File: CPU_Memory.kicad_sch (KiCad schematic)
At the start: 1 part

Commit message: Added LGA1151 socket bracket holes
stolen from another lga1151 footprint that has wrong pin numbers....
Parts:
- JCPU1: footprint A-my-stuff:LGA-1151_L47.1-W42.5-P0.91_PE115127-4041-01H -> A-my-stuff:LGA1151_TE-2287402-1
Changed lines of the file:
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@@
 			)
 		)
-		(property "Footprint" "A-my-stuff:LGA-1151_L47.1-W42.5-P0.91_PE115127-4041-01H"
+		(property "Footprint" "A-my-stuff:LGA1151_TE-2287402-1"
 			(at 107.95 246.38 0)
 			(effects
@@
 			)
 		)
-		(property "Footprint" "A-my-stuff:LGA-1151_L47.1-W42.5-P0.91_PE115127-4041-01H"
+		(property "Footprint" "A-my-stuff:LGA1151_TE-2287402-1"
 			(at 273.05 246.38 0)
 			(effects

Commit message: Added CPU CFG resistors
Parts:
- JCPU1: footprint A-my-stuff:LGA1151_TE-2287402-1 -> A-my-stuff:LGA-1151_L47.1-W42.5-P0.91_PE115127-4041-01H
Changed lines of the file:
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@@
 			)
 		)
-		(property "Footprint" "A-my-stuff:LGA1151_TE-2287402-1"
+		(property "Footprint" "A-my-stuff:LGA-1151_L47.1-W42.5-P0.91_PE115127-4041-01H"
 			(at 107.95 246.38 0)
 			(effects
@@
 			)
 		)
-		(property "Footprint" "A-my-stuff:LGA1151_TE-2287402-1"
+		(property "Footprint" "A-my-stuff:LGA-1151_L47.1-W42.5-P0.91_PE115127-4041-01H"
 			(at 273.05 246.38 0)
 			(effects

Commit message: stroopwafel.exe
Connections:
- net DDR4_CH1_A0: now also JCPU1.AW15 (DDR0_MA_0); no longer JCPU1.AL19 (DDR1_MA_0)
- net DDR4_CH1_A1: now also JCPU1.AU18 (DDR0_MA_1); no longer JCPU1.AL22 (DDR1_MA_1)
- net DDR4_CH1_A10: now also JCPU1.AY14 (DDR0_MA_10); no longer JCPU1.AP18 (DDR1_MA_10)
- net DDR4_CH1_A11: now also JCPU1.AU22 (DDR0_MA_11); no longer JCPU1.AU27 (DDR1_MA_11)
- net DDR4_CH1_A12: now also JCPU1.AV22 (DDR0_MA_12); no longer JCPU1.AV27 (DDR1_MA_12)
- net DDR4_CH1_A13: now also JCPU1.AV12 (DDR0_MA_13); no longer JCPU1.AR15 (DDR1_MA_13)
- net DDR4_CH1_A14_WE#: now also JCPU1.AV14 (DDR0_MA_14); no longer JCPU1.AL17 (DDR1_MA_14)
- net DDR4_CH1_A15_CAS#: now also JCPU1.AY11 (DDR0_MA_15); no longer JCPU1.AP16 (DDR1_MA_15)
- net DDR4_CH1_A16_RAS#: now also JCPU1.AW13 (DDR0_MA_16); no longer JCPU1.AN18 (DDR1_MA_16)
- net DDR4_CH1_A2: now also JCPU1.AU17 (DDR0_MA_2); no longer JCPU1.AM22 (DDR1_MA_2)
- net DDR4_CH1_A3: now also JCPU1.AV19 (DDR0_MA_3); no longer JCPU1.AM23 (DDR1_MA_3)
- net DDR4_CH1_A4: now also JCPU1.AT19 (DDR0_MA_4); no longer JCPU1.AP23 (DDR1_MA_4)
- net DDR4_CH1_A5: now also JCPU1.AU20 (DDR0_MA_5); no longer JCPU1.AL23 (DDR1_MA_5)
- net DDR4_CH1_A6: now also JCPU1.AV20 (DDR0_MA_6); no longer JCPU1.AW26 (DDR1_MA_6)
- net DDR4_CH1_A7: now also JCPU1.AU21 (DDR0_MA_7); no longer JCPU1.AY26 (DDR1_MA_7)
- net DDR4_CH1_A8: now also JCPU1.AT20 (DDR0_MA_8); no longer JCPU1.AU26 (DDR1_MA_8)
- net DDR4_CH1_A9: now also JCPU1.AT22 (DDR0_MA_9); no longer JCPU1.AW27 (DDR1_MA_9)
- net DDR4_CH1_ACT#: now also JCPU1.AU24 (DDR0_ACT#); no longer JCPU1.AU28 (DDR1_ACT#)
- net DDR4_CH1_Alert#: now also JCPU1.AT23 (DDR0_ALERT#); no longer JCPU1.AY25 (DDR1_ALERT#)
- net DDR4_CH1_BA0: now also JCPU1.AY13 (DDR0_BA_0); no longer JCPU1.AL18 (DDR1_BA_0)
- net DDR4_CH1_BA1: now also JCPU1.AV15 (DDR0_BA_1); no longer JCPU1.AM18 (DDR1_BA_1)
- net DDR4_CH1_BG0: now also JCPU1.AW23 (DDR0_BG_0); no longer JCPU1.AW28 (DDR1_BG_0)
- net DDR4_CH1_BG1: now also JCPU1.AV23 (DDR0_BG_1); no longer JCPU1.AY28 (DDR1_BG_1)
- net DDR4_CH1_CKE0: now also JCPU1.AY24 (DDR0_CKE_0); no longer JCPU1.AY29 (DDR1_CKE_0)
- net DDR4_CH1_CKE1: now also JCPU1.AW24 (DDR0_CKE_1); no longer JCPU1.AV29 (DDR1_CKE_1)
- net DDR4_CH1_CLK0+: now also JCPU1.AW18 (DDR0_CKP_0); no longer JCPU1.AM20 (DDR1_CKP_0)
- net DDR4_CH1_CLK0-: now also JCPU1.AV18 (DDR0_CKN_0); no longer JCPU1.AM21 (DDR1_CKN_0)
- net DDR4_CH1_CLK1+: now also JCPU1.AW17 (DDR0_CKP_1); no longer JCPU1.AP22 (DDR1_CKP_1)
- net DDR4_CH1_CLK1-: now also JCPU1.AY17 (DDR0_CKN_1); no longer JCPU1.AP21 (DDR1_CKN_1)
- net DDR4_CH1_CS0#: now also JCPU1.AW12 (DDR0_CS#_0); no longer JCPU1.AP17 (DDR1_CS#_0)
- net DDR4_CH1_CS1#: now also JCPU1.AU11 (DDR0_CS#_1); no longer JCPU1.AN15 (DDR1_CS#_1)
- net DDR4_CH1_DQ0: now also JCPU1.AE38 (DDR0_DQ_0/DDR0_DQ_0); no longer JCPU1.AD34 (DDR1_DQ_0/DDR0_DQ_16)
- net DDR4_CH1_DQ1: now also JCPU1.AE37 (DDR0_DQ_1/DDR0_DQ_1); no longer JCPU1.AD35 (DDR1_DQ_1/DDR0_DQ_17)
- net DDR4_CH1_DQ10: now also JCPU1.AL38 (DDR0_DQ_10/DDR0_DQ_10); no longer JCPU1.AK32 (DDR1_DQ_10/DDR0_DQ_26)
- net DDR4_CH1_DQ11: now also JCPU1.AL37 (DDR0_DQ_11/DDR0_DQ_11); no longer JCPU1.AL32 (DDR1_DQ_11/DDR0_DQ_27)
- net DDR4_CH1_DQ12: now also JCPU1.AJ40 (DDR0_DQ_12/DDR0_DQ_12); no longer JCPU1.AK34 (DDR1_DQ_12/DDR0_DQ_28)
- net DDR4_CH1_DQ13: now also JCPU1.AJ39 (DDR0_DQ_13/DDR0_DQ_13); no longer JCPU1.AL34 (DDR1_DQ_13/DDR0_DQ_29)
- net DDR4_CH1_DQ14: now also JCPU1.AL39 (DDR0_DQ_14/DDR0_DQ_14); no longer JCPU1.AK31 (DDR1_DQ_14/DDR0_DQ_30)
- net DDR4_CH1_DQ15: now also JCPU1.AL40 (DDR0_DQ_15/DDR0_DQ_15); no longer JCPU1.AL31 (DDR1_DQ_15/DDR0_DQ_31)
- net DDR4_CH1_DQ16: now also JCPU1.AN38 (DDR0_DQ_16/DDR0_DQ_32); no longer JCPU1.AP35 (DDR1_DQ_16/DDR0_DQ_48)
- net DDR4_CH1_DQ17: now also JCPU1.AN40 (DDR0_DQ_17/DDR0_DQ_33); no longer JCPU1.AN35 (DDR1_DQ_17/DDR0_DQ_49)
- net DDR4_CH1_DQ18: now also JCPU1.AR38 (DDR0_DQ_18/DDR0_DQ_34); no longer JCPU1.AN32 (DDR1_DQ_18/DDR0_DQ_50)
- net DDR4_CH1_DQ19: now also JCPU1.AR37 (DDR0_DQ_19/DDR0_DQ_35); no longer JCPU1.AP32 (DDR1_DQ_19/DDR0_DQ_51)
- net DDR4_CH1_DQ2: now also JCPU1.AG38 (DDR0_DQ_2/DDR0_DQ_2); no longer JCPU1.AG35 (DDR1_DQ_2/DDR0_DQ_18)
- net DDR4_CH1_DQ20: now also JCPU1.AN39 (DDR0_DQ_20/DDR0_DQ_36); no longer JCPU1.AN34 (DDR1_DQ_20/DDR0_DQ_52)
- net DDR4_CH1_DQ21: now also JCPU1.AN37 (DDR0_DQ_21/DDR0_DQ_37); no longer JCPU1.AP34 (DDR1_DQ_21/DDR0_DQ_53)
- net DDR4_CH1_DQ22: now also JCPU1.AR39 (DDR0_DQ_22/DDR0_DQ_38); no longer JCPU1.AN31 (DDR1_DQ_22/DDR0_DQ_54)
- net DDR4_CH1_DQ23: now also JCPU1.AR40 (DDR0_DQ_23/DDR0_DQ_39); no longer JCPU1.AP31 (DDR1_DQ_23/DDR0_DQ_55)
- net DDR4_CH1_DQ24: now also JCPU1.AW37 (DDR0_DQ_24/DDR0_DQ_40); no longer JCPU1.AL29 (DDR1_DQ_24/DDR0_DQ_56)
- net DDR4_CH1_DQ25: now also JCPU1.AU38 (DDR0_DQ_25/DDR0_DQ_41); no longer JCPU1.AM29 (DDR1_DQ_25/DDR0_DQ_57)
- net DDR4_CH1_DQ26: now also JCPU1.AV35 (DDR0_DQ_26/DDR0_DQ_42); no longer JCPU1.AP29 (DDR1_DQ_26/DDR0_DQ_58)
- net DDR4_CH1_DQ27: now also JCPU1.AW35 (DDR0_DQ_27/DDR0_DQ_43); no longer JCPU1.AR29 (DDR1_DQ_27/DDR0_DQ_59)
- net DDR4_CH1_DQ28: now also JCPU1.AU37 (DDR0_DQ_28/DDR0_DQ_44); no longer JCPU1.AM28 (DDR1_DQ_28/DDR0_DQ_60)
- net DDR4_CH1_DQ29: now also JCPU1.AV37 (DDR0_DQ_29/DDR0_DQ_45); no longer JCPU1.AL28 (DDR1_DQ_29/DDR0_DQ_61)
- net DDR4_CH1_DQ3: now also JCPU1.AG37 (DDR0_DQ_3/DDR0_DQ_3); no longer JCPU1.AH35 (DDR1_DQ_3/DDR0_DQ_19)
- net DDR4_CH1_DQ30: now also JCPU1.AT35 (DDR0_DQ_30/DDR0_DQ_46); no longer JCPU1.AR28 (DDR1_DQ_30/DDR0_DQ_62)
- net DDR4_CH1_DQ31: now also JCPU1.AU35 (DDR0_DQ_31/DDR0_DQ_47); no longer JCPU1.AP28 (DDR1_DQ_31/DDR0_DQ_63)
- net DDR4_CH1_DQ32: now also JCPU1.AY8 (DDR0_DQ_32/DDR1_DQ_0); no longer JCPU1.AR12 (DDR1_DQ_32/DDR1_DQ_16)
- net DDR4_CH1_DQ33: now also JCPU1.AW8 (DDR0_DQ_33/DDR1_DQ_1); no longer JCPU1.AP12 (DDR1_DQ_33/DDR1_DQ_17)
- net DDR4_CH1_DQ34: now also JCPU1.AV6 (DDR0_DQ_34/DDR1_DQ_2); no longer JCPU1.AM13 (DDR1_DQ_34/DDR1_DQ_18)
- net DDR4_CH1_DQ35: now also JCPU1.AU6 (DDR0_DQ_35/DDR1_DQ_3); no longer JCPU1.AL13 (DDR1_DQ_35/DDR1_DQ_19)
- net DDR4_CH1_DQ36: now also JCPU1.AU8 (DDR0_DQ_36/DDR1_DQ_4); no longer JCPU1.AR13 (DDR1_DQ_36/DDR1_DQ_20)
- net DDR4_CH1_DQ37: now also JCPU1.AV8 (DDR0_DQ_37/DDR1_DQ_5); no longer JCPU1.AP13 (DDR1_DQ_37/DDR1_DQ_21)
- net DDR4_CH1_DQ38: now also JCPU1.AW6 (DDR0_DQ_38/DDR1_DQ_6); no longer JCPU1.AM12 (DDR1_DQ_38/DDR1_DQ_22)
- net DDR4_CH1_DQ39: now also JCPU1.AY6 (DDR0_DQ_39/DDR1_DQ_7); no longer JCPU1.AL12 (DDR1_DQ_39/DDR1_DQ_23)
- net DDR4_CH1_DQ4: now also JCPU1.AE39 (DDR0_DQ_4/DDR0_DQ_4); no longer JCPU1.AE35 (DDR1_DQ_4/DDR0_DQ_20)
- net DDR4_CH1_DQ40: now also JCPU1.AY4 (DDR0_DQ_40/DDR1_DQ_8); no longer JCPU1.AP10 (DDR1_DQ_40/DDR1_DQ_24)
- net DDR4_CH1_DQ41: now also JCPU1.AV4 (DDR0_DQ_41/DDR1_DQ_9); no longer JCPU1.AR10 (DDR1_DQ_41/DDR1_DQ_25)
- net DDR4_CH1_DQ42: now also JCPU1.AT1 (DDR0_DQ_42/DDR1_DQ_10); no longer JCPU1.AR7 (DDR1_DQ_42/DDR1_DQ_26)
- net DDR4_CH1_DQ43: now also JCPU1.AT2 (DDR0_DQ_43/DDR1_DQ_11); no longer JCPU1.AP7 (DDR1_DQ_43/DDR1_DQ_27)
- net DDR4_CH1_DQ44: now also JCPU1.AV3 (DDR0_DQ_44/DDR1_DQ_12); no longer JCPU1.AR9 (DDR1_DQ_44/DDR1_DQ_28)
- net DDR4_CH1_DQ45: now also JCPU1.AW4 (DDR0_DQ_45/DDR1_DQ_13); no longer JCPU1.AP9 (DDR1_DQ_45/DDR1_DQ_29)
- net DDR4_CH1_DQ46: now also JCPU1.AT4 (DDR0_DQ_46/DDR1_DQ_14); no longer JCPU1.AR6 (DDR1_DQ_46/DDR1_DQ_30)
- net DDR4_CH1_DQ47: now also JCPU1.AT3 (DDR0_DQ_47/DDR1_DQ_15); no longer JCPU1.AP6 (DDR1_DQ_47/DDR1_DQ_31)
- net DDR4_CH1_DQ48: now also JCPU1.AP2 (DDR0_DQ_48/DDR1_DQ_32); no longer JCPU1.AM10 (DDR1_DQ_48/DDR1_DQ_48)
- net DDR4_CH1_DQ49: now also JCPU1.AM4 (DDR0_DQ_49/DDR1_DQ_33); no longer JCPU1.AL10 (DDR1_DQ_49/DDR1_DQ_49)
- net DDR4_CH1_DQ5: now also JCPU1.AE40 (DDR0_DQ_5/DDR0_DQ_5); no longer JCPU1.AE34 (DDR1_DQ_5/DDR0_DQ_21)
- net DDR4_CH1_DQ50: now also JCPU1.AP3 (DDR0_DQ_50/DDR1_DQ_34); no longer JCPU1.AM7 (DDR1_DQ_50/DDR1_DQ_50)
- net DDR4_CH1_DQ51: now also JCPU1.AM3 (DDR0_DQ_51/DDR1_DQ_35); no longer JCPU1.AL7 (DDR1_DQ_51/DDR1_DQ_51)
- net DDR4_CH1_DQ52: now also JCPU1.AP4 (DDR0_DQ_52/DDR1_DQ_36); no longer JCPU1.AM9 (DDR1_DQ_52/DDR1_DQ_52)
- net DDR4_CH1_DQ53: now also JCPU1.AM2 (DDR0_DQ_53/DDR1_DQ_37); no longer JCPU1.AL9 (DDR1_DQ_53/DDR1_DQ_53)
- net DDR4_CH1_DQ54: now also JCPU1.AP1 (DDR0_DQ_54/DDR1_DQ_38); no longer JCPU1.AM6 (DDR1_DQ_54/DDR1_DQ_54)
- net DDR4_CH1_DQ55: now also JCPU1.AM1 (DDR0_DQ_55/DDR1_DQ_39); no longer JCPU1.AL6 (DDR1_DQ_55/DDR1_DQ_55)
- net DDR4_CH1_DQ56: now also JCPU1.AK3 (DDR0_DQ_56/DDR1_DQ_40); no longer JCPU1.AJ6 (DDR1_DQ_56/DDR1_DQ_56)
- net DDR4_CH1_DQ57: now also JCPU1.AH1 (DDR0_DQ_57/DDR1_DQ_41); no longer JCPU1.AJ7 (DDR1_DQ_57/DDR1_DQ_57)
- net DDR4_CH1_DQ58: now also JCPU1.AK4 (DDR0_DQ_58/DDR1_DQ_42); no longer JCPU1.AE6 (DDR1_DQ_58/DDR1_DQ_58)
- net DDR4_CH1_DQ59: now also JCPU1.AH2 (DDR0_DQ_59/DDR1_DQ_43); no longer JCPU1.AF7 (DDR1_DQ_59/DDR1_DQ_59)
- net DDR4_CH1_DQ6: now also JCPU1.AG39 (DDR0_DQ_6/DDR0_DQ_6); no longer JCPU1.AG34 (DDR1_DQ_6/DDR0_DQ_22)
- net DDR4_CH1_DQ60: now also JCPU1.AH4 (DDR0_DQ_60/DDR1_DQ_44); no longer JCPU1.AH7 (DDR1_DQ_60/DDR1_DQ_60)
- net DDR4_CH1_DQ61: now also JCPU1.AK2 (DDR0_DQ_61/DDR1_DQ_45); no longer JCPU1.AH6 (DDR1_DQ_61/DDR1_DQ_61)
- net DDR4_CH1_DQ62: now also JCPU1.AH3 (DDR0_DQ_62/DDR1_DQ_46); no longer JCPU1.AE7 (DDR1_DQ_62/DDR1_DQ_62)
- net DDR4_CH1_DQ63: now also JCPU1.AK1 (DDR0_DQ_63/DDR1_DQ_47); no longer JCPU1.AF6 (DDR1_DQ_63/DDR1_DQ_63)
- net DDR4_CH1_DQ7: now also JCPU1.AG40 (DDR0_DQ_7/DDR0_DQ_7); no longer JCPU1.AH34 (DDR1_DQ_7/DDR0_DQ_23)
- net DDR4_CH1_DQ8: now also JCPU1.AJ38 (DDR0_DQ_8/DDR0_DQ_8); no longer JCPU1.AK35 (DDR1_DQ_8/DDR0_DQ_24)
- net DDR4_CH1_DQ9: now also JCPU1.AJ37 (DDR0_DQ_9/DDR0_DQ_9); no longer JCPU1.AL35 (DDR1_DQ_9/DDR0_DQ_25)
- net DDR4_CH1_DQS0+: now also JCPU1.AF38 (DDR0_DQSP_0/DDR0_DQSP_0); no longer JCPU1.AF35 (DDR1_DQSP_0/DDR0_DQSP_2)
- net DDR4_CH1_DQS0-: now also JCPU1.AF39 (DDR0_DQSN_0/DDR0_DQSN_0); no longer JCPU1.AF34 (DDR1_DQSN_0/DDR0_DQSN_2)
- net DDR4_CH1_DQS1+: now also JCPU1.AK38 (DDR0_DQSP_1/DDR0_DQSP_1); no longer JCPU1.AL33 (DDR1_DQSP_1/DDR0_DQSP_3)
- net DDR4_CH1_DQS1-: now also JCPU1.AK39 (DDR0_DQSN_1/DDR0_DQSN_1); no longer JCPU1.AK33 (DDR1_DQSN_1/DDR0_DQSN_3)
- net DDR4_CH1_DQS2+: now also JCPU1.AP38 (DDR0_DQSP_2/DDR0_DQSP_4); no longer JCPU1.AP33 (DDR1_DQSP_2/DDR0_DQSP_6)
- net DDR4_CH1_DQS2-: now also JCPU1.AP39 (DDR0_DQSN_2/DDR0_DQSN_4); no longer JCPU1.AN33 (DDR1_DQSN_2/DDR0_DQSN_6)
- net DDR4_CH1_DQS3+: now also JCPU1.AV36 (DDR0_DQSP_3/DDR0_DQSP_5); no longer JCPU1.AN28 (DDR1_DQSP_3/DDR0_DQSP_7)
- net DDR4_CH1_DQS3-: now also JCPU1.AU36 (DDR0_DQSN_3/DDR0_DQSN_5); no longer JCPU1.AN29 (DDR1_DQSN_3/DDR0_DQSN_7)
- net DDR4_CH1_DQS4+: now also JCPU1.AV7 (DDR0_DQSP_4/DDR1_DQSP_0); no longer JCPU1.AN12 (DDR1_DQSP_4/DDR1_DQSP_2)
- net DDR4_CH1_DQS4-: now also JCPU1.AW7 (DDR0_DQSN_4/DDR1_DQSN_0); no longer JCPU1.AN13 (DDR1_DQSN_4/DDR1_DQSN_2)
- net DDR4_CH1_DQS5+: now also JCPU1.AU2 (DDR0_DQSP_5/DDR1_DQSP_1); no longer JCPU1.AP8 (DDR1_DQSP_5/DDR1_DQSP_3)
- net DDR4_CH1_DQS5-: now also JCPU1.AU3 (DDR0_DQSN_5/DDR1_DQSN_1); no longer JCPU1.AR8 (DDR1_DQSN_5/DDR1_DQSN_3)
- net DDR4_CH1_DQS6+: now also JCPU1.AN2 (DDR0_DQSP_6/DDR1_DQSP_4); no longer JCPU1.AL8 (DDR1_DQSP_6/DDR1_DQSP_6)
- net DDR4_CH1_DQS6-: now also JCPU1.AN3 (DDR0_DQSN_6/DDR1_DQSN_4); no longer JCPU1.AM8 (DDR1_DQSN_6/DDR1_DQSN_6)
- net DDR4_CH1_DQS7+: now also JCPU1.AJ2 (DDR0_DQSP_7/DDR1_DQSP_5); no longer JCPU1.AG7 (DDR1_DQSP_7/DDR1_DQSP_7)
- net DDR4_CH1_DQS7-: now also JCPU1.AJ3 (DDR0_DQSN_7/DDR1_DQSN_5); no longer JCPU1.AG6 (DDR1_DQSN_7/DDR1_DQSN_7)
- net DDR4_CH1_DQS8+: now also JCPU1.AV32 (DDR0_DQSP_8/DDR0_DQSP_8); no longer JCPU1.AN25 (DDR1_DQSP_8/DDR1_DQSP_8)
- net DDR4_CH1_DQS8-: now also JCPU1.AU32 (DDR0_DQSN_8/DDR0_DQSN_8); no longer JCPU1.AN26 (DDR1_DQSN_8/DDR1_DQSN_8)
- net DDR4_CH1_ECC0: now also JCPU1.AU33 (DDR0_ECC_0); no longer JCPU1.AR25 (DDR1_ECC_0)
- net DDR4_CH1_ECC1: now also JCPU1.AT33 (DDR0_ECC_1); no longer JCPU1.AR26 (DDR1_ECC_1)
- net DDR4_CH1_ECC2: now also JCPU1.AW33 (DDR0_ECC_2); no longer JCPU1.AM26 (DDR1_ECC_2)
- net DDR4_CH1_ECC3: now also JCPU1.AV31 (DDR0_ECC_3); no longer JCPU1.AM25 (DDR1_ECC_3)
- net DDR4_CH1_ECC4: now also JCPU1.AU31 (DDR0_ECC_4); no longer JCPU1.AP26 (DDR1_ECC_4)
- net DDR4_CH1_ECC5: now also JCPU1.AV33 (DDR0_ECC_5); no longer JCPU1.AP25 (DDR1_ECC_5)
- net DDR4_CH1_ECC6: now also JCPU1.AW31 (DDR0_ECC_6); no longer JCPU1.AL25 (DDR1_ECC_6)
- net DDR4_CH1_ECC7: now also JCPU1.AY31 (DDR0_ECC_7); no longer JCPU1.AL26 (DDR1_ECC_7)
- net DDR4_CH1_ODT0: now also JCPU1.AW11 (DDR0_ODT_0); no longer JCPU1.AM16 (DDR1_ODT_0)
- net DDR4_CH1_ODT1: now also JCPU1.AU14 (DDR0_ODT_1); no longer JCPU1.AL16 (DDR1_ODT_1)
- net DDR4_CH1_Parity: now also JCPU1.AY15 (DDR0_PAR); no longer JCPU1.AL20 (DDR1_PAR)
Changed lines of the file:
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@@
 		(pin "J5"
-		)
-		(instances
-			(project ""
-				(path "/4bc771b8-eb19-46d0-8798-27231a7c6e83/061fe2d6-87c2-48c2-90bb-0928700512fc"
-					(reference "JCPU1")
-					(unit 1)
-				)
-				(path "/4bc771b8-eb19-46d0-8798-27231a7c6e83/deeadc73-acb4-40d7-9415-61f11f304ecd"
-					(reference "JCPU1")
-					(unit 1)
-				)
-			)
 		)
 	)
@@
 		(lib_id "A-my-stuff:Intel_CFL_1151")
 		(at 273.05 134.62 0)
-		(unit 2)
+		(unit 1)
 		(exclude_from_sim no)
 		(in_bom yes)
@@
 		(pin "J5"
 		)
-		(instances
-			(project ""
-				(path "/4bc771b8-eb19-46d0-8798-27231a7c6e83/061fe2d6-87c2-48c2-90bb-0928700512fc"
-					(reference "JCPU1")
-					(unit 2)
-				)
-				(path "/4bc771b8-eb19-46d0-8798-27231a7c6e83/deeadc73-acb4-40d7-9415-61f11f304ecd"
-					(reference "JCPU1")
-					(unit 2)
-				)
-			)
-		)
 	)

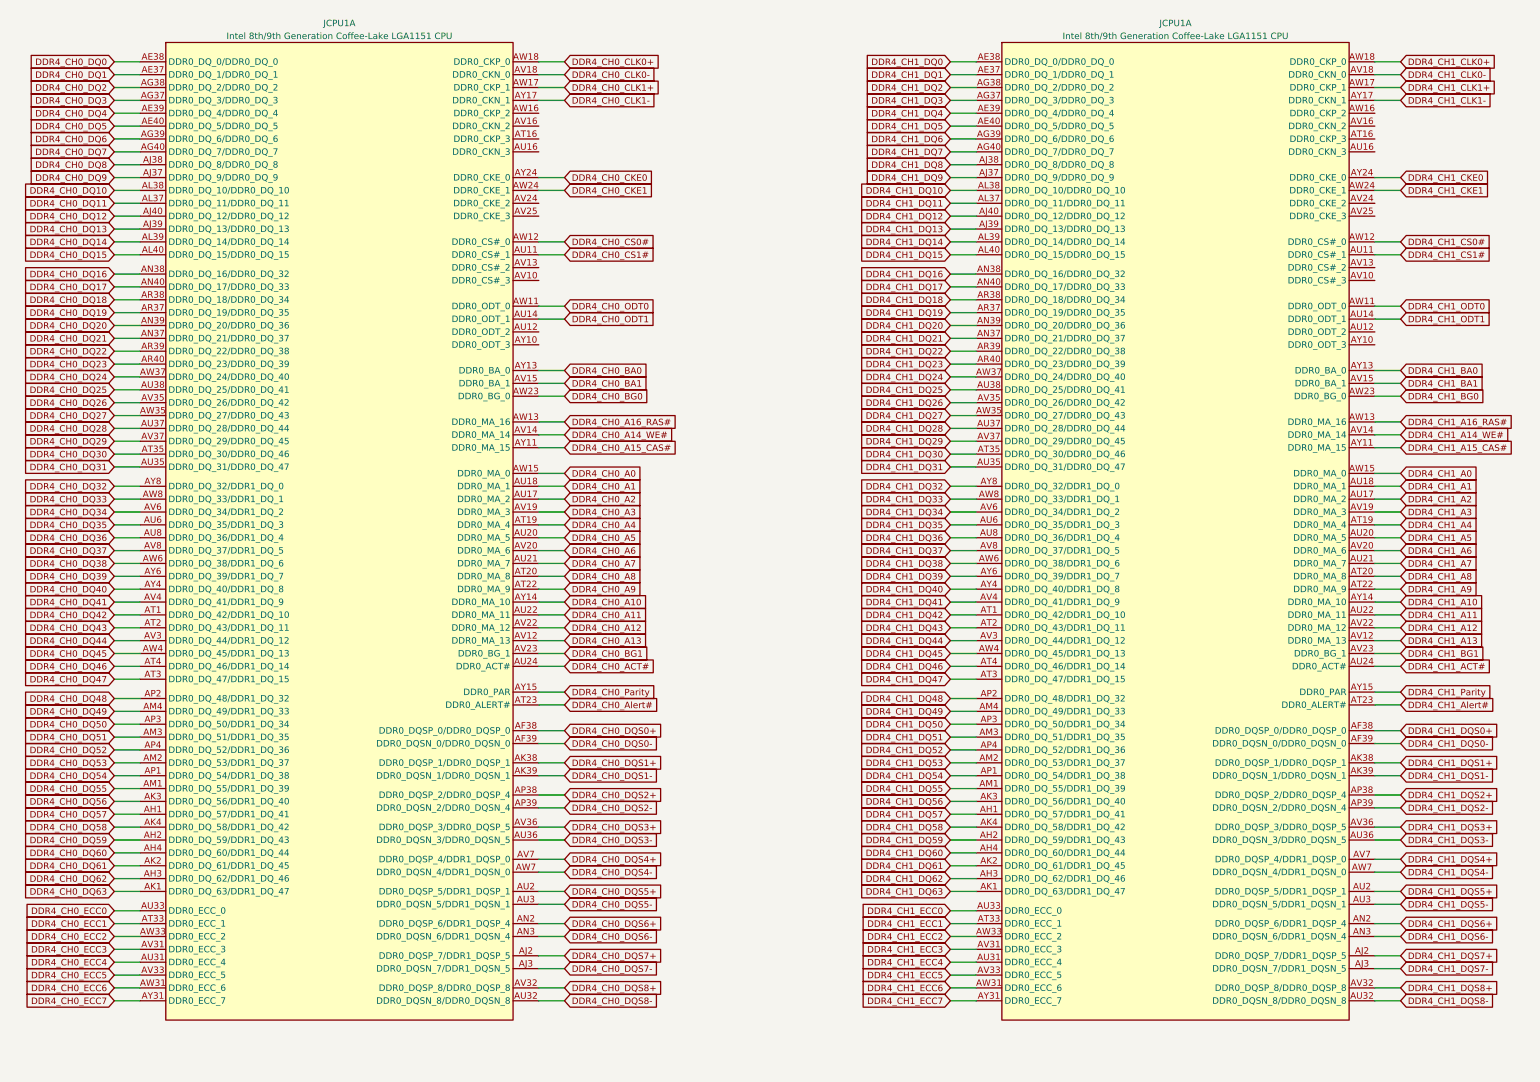
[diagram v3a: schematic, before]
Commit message: Fixed entire schematic being broken
somehow every symbol with index 1 broke and updating the pcb stopped working. how does that even happen. oh well it's fixed now
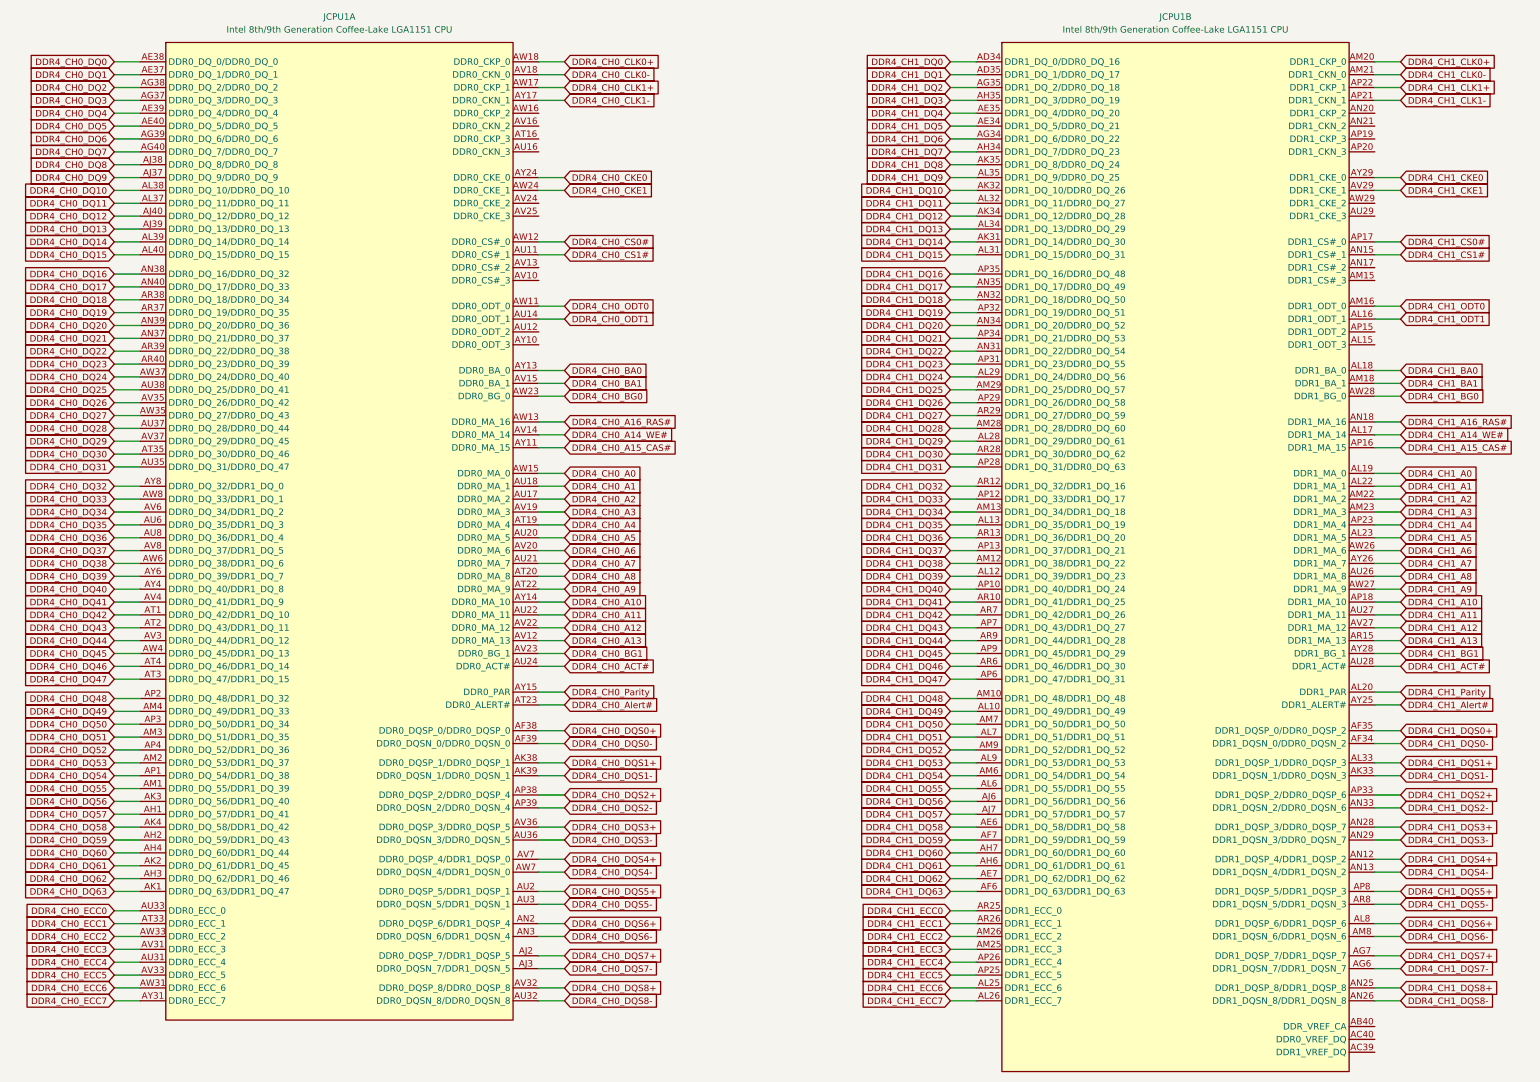
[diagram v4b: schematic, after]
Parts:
- removed JCPU1 (x2): Intel 8th/9th Generation Coffee-Lake LGA1151 CPU, A-my-stuff:LGA-1151_L47.1-W42.5-P0.91_PE115127-4041-01H, symbol A-my-stuff:Intel_CFL_1151
- added JCPU1: Intel 8th/9th Generation Coffee-Lake LGA1151 CPU, A-my-stuff:LGA-1151_L47.1-W42.5-P0.91_PE115127-4041-01H, symbol A-my-stuff:Intel_CFL_1151
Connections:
- net DDR4_CH0_A0: now also JCPU1.AW15 (DDR0_MA_0)
- net DDR4_CH0_A1: now also JCPU1.AU18 (DDR0_MA_1)
- net DDR4_CH0_A10: now also JCPU1.AY14 (DDR0_MA_10)
- net DDR4_CH0_A11: now also JCPU1.AU22 (DDR0_MA_11)
- net DDR4_CH0_A12: now also JCPU1.AV22 (DDR0_MA_12)
- net DDR4_CH0_A13: now also JCPU1.AV12 (DDR0_MA_13)
- net DDR4_CH0_A14_WE#: now also JCPU1.AV14 (DDR0_MA_14)
- net DDR4_CH0_A15_CAS#: now also JCPU1.AY11 (DDR0_MA_15)
- net DDR4_CH0_A16_RAS#: now also JCPU1.AW13 (DDR0_MA_16)
- net DDR4_CH0_A2: now also JCPU1.AU17 (DDR0_MA_2)
- net DDR4_CH0_A3: now also JCPU1.AV19 (DDR0_MA_3)
- net DDR4_CH0_A4: now also JCPU1.AT19 (DDR0_MA_4)
- net DDR4_CH0_A5: now also JCPU1.AU20 (DDR0_MA_5)
- net DDR4_CH0_A6: now also JCPU1.AV20 (DDR0_MA_6)
- net DDR4_CH0_A7: now also JCPU1.AU21 (DDR0_MA_7)
- net DDR4_CH0_A8: now also JCPU1.AT20 (DDR0_MA_8)
- net DDR4_CH0_A9: now also JCPU1.AT22 (DDR0_MA_9)
- net DDR4_CH0_ACT#: now also JCPU1.AU24 (DDR0_ACT#)
- net DDR4_CH0_Alert#: now also JCPU1.AT23 (DDR0_ALERT#)
- net DDR4_CH0_BA0: now also JCPU1.AY13 (DDR0_BA_0)
- net DDR4_CH0_BA1: now also JCPU1.AV15 (DDR0_BA_1)
- net DDR4_CH0_BG0: now also JCPU1.AW23 (DDR0_BG_0)
- net DDR4_CH0_BG1: now also JCPU1.AV23 (DDR0_BG_1)
- net DDR4_CH0_CKE0: now also JCPU1.AY24 (DDR0_CKE_0)
- net DDR4_CH0_CKE1: now also JCPU1.AW24 (DDR0_CKE_1)
- net DDR4_CH0_CLK0+: now also JCPU1.AW18 (DDR0_CKP_0)
- net DDR4_CH0_CLK0-: now also JCPU1.AV18 (DDR0_CKN_0)
- net DDR4_CH0_CLK1+: now also JCPU1.AW17 (DDR0_CKP_1)
- net DDR4_CH0_CLK1-: now also JCPU1.AY17 (DDR0_CKN_1)
- net DDR4_CH0_CS0#: now also JCPU1.AW12 (DDR0_CS#_0)
- net DDR4_CH0_CS1#: now also JCPU1.AU11 (DDR0_CS#_1)
- net DDR4_CH0_DQ0: now also JCPU1.AE38 (DDR0_DQ_0/DDR0_DQ_0)
- net DDR4_CH0_DQ1: now also JCPU1.AE37 (DDR0_DQ_1/DDR0_DQ_1)
- net DDR4_CH0_DQ10: now also JCPU1.AL38 (DDR0_DQ_10/DDR0_DQ_10)
- net DDR4_CH0_DQ11: now also JCPU1.AL37 (DDR0_DQ_11/DDR0_DQ_11)
- net DDR4_CH0_DQ12: now also JCPU1.AJ40 (DDR0_DQ_12/DDR0_DQ_12)
- net DDR4_CH0_DQ13: now also JCPU1.AJ39 (DDR0_DQ_13/DDR0_DQ_13)
- net DDR4_CH0_DQ14: now also JCPU1.AL39 (DDR0_DQ_14/DDR0_DQ_14)
- net DDR4_CH0_DQ15: now also JCPU1.AL40 (DDR0_DQ_15/DDR0_DQ_15)
- net DDR4_CH0_DQ16: now also JCPU1.AN38 (DDR0_DQ_16/DDR0_DQ_32)
- net DDR4_CH0_DQ17: now also JCPU1.AN40 (DDR0_DQ_17/DDR0_DQ_33)
- net DDR4_CH0_DQ18: now also JCPU1.AR38 (DDR0_DQ_18/DDR0_DQ_34)
- net DDR4_CH0_DQ19: now also JCPU1.AR37 (DDR0_DQ_19/DDR0_DQ_35)
- net DDR4_CH0_DQ2: now also JCPU1.AG38 (DDR0_DQ_2/DDR0_DQ_2)
- net DDR4_CH0_DQ20: now also JCPU1.AN39 (DDR0_DQ_20/DDR0_DQ_36)
- net DDR4_CH0_DQ21: now also JCPU1.AN37 (DDR0_DQ_21/DDR0_DQ_37)
- net DDR4_CH0_DQ22: now also JCPU1.AR39 (DDR0_DQ_22/DDR0_DQ_38)
- net DDR4_CH0_DQ23: now also JCPU1.AR40 (DDR0_DQ_23/DDR0_DQ_39)
- net DDR4_CH0_DQ24: now also JCPU1.AW37 (DDR0_DQ_24/DDR0_DQ_40)
- net DDR4_CH0_DQ25: now also JCPU1.AU38 (DDR0_DQ_25/DDR0_DQ_41)
- net DDR4_CH0_DQ26: now also JCPU1.AV35 (DDR0_DQ_26/DDR0_DQ_42)
- net DDR4_CH0_DQ27: now also JCPU1.AW35 (DDR0_DQ_27/DDR0_DQ_43)
- net DDR4_CH0_DQ28: now also JCPU1.AU37 (DDR0_DQ_28/DDR0_DQ_44)
- net DDR4_CH0_DQ29: now also JCPU1.AV37 (DDR0_DQ_29/DDR0_DQ_45)
- net DDR4_CH0_DQ3: now also JCPU1.AG37 (DDR0_DQ_3/DDR0_DQ_3)
- net DDR4_CH0_DQ30: now also JCPU1.AT35 (DDR0_DQ_30/DDR0_DQ_46)
- net DDR4_CH0_DQ31: now also JCPU1.AU35 (DDR0_DQ_31/DDR0_DQ_47)
- net DDR4_CH0_DQ32: now also JCPU1.AY8 (DDR0_DQ_32/DDR1_DQ_0)
- net DDR4_CH0_DQ33: now also JCPU1.AW8 (DDR0_DQ_33/DDR1_DQ_1)
- net DDR4_CH0_DQ34: now also JCPU1.AV6 (DDR0_DQ_34/DDR1_DQ_2)
- net DDR4_CH0_DQ35: now also JCPU1.AU6 (DDR0_DQ_35/DDR1_DQ_3)
- net DDR4_CH0_DQ36: now also JCPU1.AU8 (DDR0_DQ_36/DDR1_DQ_4)
- net DDR4_CH0_DQ37: now also JCPU1.AV8 (DDR0_DQ_37/DDR1_DQ_5)
- net DDR4_CH0_DQ38: now also JCPU1.AW6 (DDR0_DQ_38/DDR1_DQ_6)
- net DDR4_CH0_DQ39: now also JCPU1.AY6 (DDR0_DQ_39/DDR1_DQ_7)
- net DDR4_CH0_DQ4: now also JCPU1.AE39 (DDR0_DQ_4/DDR0_DQ_4)
- net DDR4_CH0_DQ40: now also JCPU1.AY4 (DDR0_DQ_40/DDR1_DQ_8)
- net DDR4_CH0_DQ41: now also JCPU1.AV4 (DDR0_DQ_41/DDR1_DQ_9)
- net DDR4_CH0_DQ42: now also JCPU1.AT1 (DDR0_DQ_42/DDR1_DQ_10)
- net DDR4_CH0_DQ43: now also JCPU1.AT2 (DDR0_DQ_43/DDR1_DQ_11)
- net DDR4_CH0_DQ44: now also JCPU1.AV3 (DDR0_DQ_44/DDR1_DQ_12)
- net DDR4_CH0_DQ45: now also JCPU1.AW4 (DDR0_DQ_45/DDR1_DQ_13)
- net DDR4_CH0_DQ46: now also JCPU1.AT4 (DDR0_DQ_46/DDR1_DQ_14)
- net DDR4_CH0_DQ47: now also JCPU1.AT3 (DDR0_DQ_47/DDR1_DQ_15)
- net DDR4_CH0_DQ48: now also JCPU1.AP2 (DDR0_DQ_48/DDR1_DQ_32)
- net DDR4_CH0_DQ49: now also JCPU1.AM4 (DDR0_DQ_49/DDR1_DQ_33)
- net DDR4_CH0_DQ5: now also JCPU1.AE40 (DDR0_DQ_5/DDR0_DQ_5)
- net DDR4_CH0_DQ50: now also JCPU1.AP3 (DDR0_DQ_50/DDR1_DQ_34)
- net DDR4_CH0_DQ51: now also JCPU1.AM3 (DDR0_DQ_51/DDR1_DQ_35)
- net DDR4_CH0_DQ52: now also JCPU1.AP4 (DDR0_DQ_52/DDR1_DQ_36)
- net DDR4_CH0_DQ53: now also JCPU1.AM2 (DDR0_DQ_53/DDR1_DQ_37)
- net DDR4_CH0_DQ54: now also JCPU1.AP1 (DDR0_DQ_54/DDR1_DQ_38)
- net DDR4_CH0_DQ55: now also JCPU1.AM1 (DDR0_DQ_55/DDR1_DQ_39)
- net DDR4_CH0_DQ56: now also JCPU1.AK3 (DDR0_DQ_56/DDR1_DQ_40)
- net DDR4_CH0_DQ57: now also JCPU1.AH1 (DDR0_DQ_57/DDR1_DQ_41)
- net DDR4_CH0_DQ58: now also JCPU1.AK4 (DDR0_DQ_58/DDR1_DQ_42)
- net DDR4_CH0_DQ59: now also JCPU1.AH2 (DDR0_DQ_59/DDR1_DQ_43)
- net DDR4_CH0_DQ6: now also JCPU1.AG39 (DDR0_DQ_6/DDR0_DQ_6)
- net DDR4_CH0_DQ60: now also JCPU1.AH4 (DDR0_DQ_60/DDR1_DQ_44)
- net DDR4_CH0_DQ61: now also JCPU1.AK2 (DDR0_DQ_61/DDR1_DQ_45)
- net DDR4_CH0_DQ62: now also JCPU1.AH3 (DDR0_DQ_62/DDR1_DQ_46)
- net DDR4_CH0_DQ63: now also JCPU1.AK1 (DDR0_DQ_63/DDR1_DQ_47)
- net DDR4_CH0_DQ7: now also JCPU1.AG40 (DDR0_DQ_7/DDR0_DQ_7)
- net DDR4_CH0_DQ8: now also JCPU1.AJ38 (DDR0_DQ_8/DDR0_DQ_8)
- net DDR4_CH0_DQ9: now also JCPU1.AJ37 (DDR0_DQ_9/DDR0_DQ_9)
- net DDR4_CH0_DQS0+: now also JCPU1.AF38 (DDR0_DQSP_0/DDR0_DQSP_0)
- net DDR4_CH0_DQS0-: now also JCPU1.AF39 (DDR0_DQSN_0/DDR0_DQSN_0)
- net DDR4_CH0_DQS1+: now also JCPU1.AK38 (DDR0_DQSP_1/DDR0_DQSP_1)
- net DDR4_CH0_DQS1-: now also JCPU1.AK39 (DDR0_DQSN_1/DDR0_DQSN_1)
- net DDR4_CH0_DQS2+: now also JCPU1.AP38 (DDR0_DQSP_2/DDR0_DQSP_4)
- net DDR4_CH0_DQS2-: now also JCPU1.AP39 (DDR0_DQSN_2/DDR0_DQSN_4)
- net DDR4_CH0_DQS3+: now also JCPU1.AV36 (DDR0_DQSP_3/DDR0_DQSP_5)
- net DDR4_CH0_DQS3-: now also JCPU1.AU36 (DDR0_DQSN_3/DDR0_DQSN_5)
- net DDR4_CH0_DQS4+: now also JCPU1.AV7 (DDR0_DQSP_4/DDR1_DQSP_0)
- net DDR4_CH0_DQS4-: now also JCPU1.AW7 (DDR0_DQSN_4/DDR1_DQSN_0)
- net DDR4_CH0_DQS5+: now also JCPU1.AU2 (DDR0_DQSP_5/DDR1_DQSP_1)
- net DDR4_CH0_DQS5-: now also JCPU1.AU3 (DDR0_DQSN_5/DDR1_DQSN_1)
- net DDR4_CH0_DQS6+: now also JCPU1.AN2 (DDR0_DQSP_6/DDR1_DQSP_4)
- net DDR4_CH0_DQS6-: now also JCPU1.AN3 (DDR0_DQSN_6/DDR1_DQSN_4)
- net DDR4_CH0_DQS7+: now also JCPU1.AJ2 (DDR0_DQSP_7/DDR1_DQSP_5)
- net DDR4_CH0_DQS7-: now also JCPU1.AJ3 (DDR0_DQSN_7/DDR1_DQSN_5)
- net DDR4_CH0_DQS8+: now also JCPU1.AV32 (DDR0_DQSP_8/DDR0_DQSP_8)
- net DDR4_CH0_DQS8-: now also JCPU1.AU32 (DDR0_DQSN_8/DDR0_DQSN_8)
- net DDR4_CH0_ECC0: now also JCPU1.AU33 (DDR0_ECC_0)
- net DDR4_CH0_ECC1: now also JCPU1.AT33 (DDR0_ECC_1)
- net DDR4_CH0_ECC2: now also JCPU1.AW33 (DDR0_ECC_2)
- net DDR4_CH0_ECC3: now also JCPU1.AV31 (DDR0_ECC_3)
- net DDR4_CH0_ECC4: now also JCPU1.AU31 (DDR0_ECC_4)
- net DDR4_CH0_ECC5: now also JCPU1.AV33 (DDR0_ECC_5)
- net DDR4_CH0_ECC6: now also JCPU1.AW31 (DDR0_ECC_6)
- net DDR4_CH0_ECC7: now also JCPU1.AY31 (DDR0_ECC_7)
- net DDR4_CH0_ODT0: now also JCPU1.AW11 (DDR0_ODT_0)
- net DDR4_CH0_ODT1: now also JCPU1.AU14 (DDR0_ODT_1)
- net DDR4_CH0_Parity: now also JCPU1.AY15 (DDR0_PAR)
- net DDR4_CH1_A0: now also JCPU1.AL19 (DDR1_MA_0)
- net DDR4_CH1_A1: now also JCPU1.AL22 (DDR1_MA_1)
- net DDR4_CH1_A10: now also JCPU1.AP18 (DDR1_MA_10)
- net DDR4_CH1_A11: now also JCPU1.AU27 (DDR1_MA_11)
- net DDR4_CH1_A12: now also JCPU1.AV27 (DDR1_MA_12)
- net DDR4_CH1_A13: now also JCPU1.AR15 (DDR1_MA_13)
- net DDR4_CH1_A14_WE#: now also JCPU1.AL17 (DDR1_MA_14)
- net DDR4_CH1_A15_CAS#: now also JCPU1.AP16 (DDR1_MA_15)
- net DDR4_CH1_A16_RAS#: now also JCPU1.AN18 (DDR1_MA_16)
- net DDR4_CH1_A2: now also JCPU1.AM22 (DDR1_MA_2)
- net DDR4_CH1_A3: now also JCPU1.AM23 (DDR1_MA_3)
- net DDR4_CH1_A4: now also JCPU1.AP23 (DDR1_MA_4)
- net DDR4_CH1_A5: now also JCPU1.AL23 (DDR1_MA_5)
- net DDR4_CH1_A6: now also JCPU1.AW26 (DDR1_MA_6)
- net DDR4_CH1_A7: now also JCPU1.AY26 (DDR1_MA_7)
- net DDR4_CH1_A8: now also JCPU1.AU26 (DDR1_MA_8)
- net DDR4_CH1_A9: now also JCPU1.AW27 (DDR1_MA_9)
- net DDR4_CH1_ACT#: now also JCPU1.AU28 (DDR1_ACT#)
- net DDR4_CH1_Alert#: now also JCPU1.AY25 (DDR1_ALERT#)
- net DDR4_CH1_BA0: now also JCPU1.AL18 (DDR1_BA_0)
- net DDR4_CH1_BA1: now also JCPU1.AM18 (DDR1_BA_1)
- net DDR4_CH1_BG0: now also JCPU1.AW28 (DDR1_BG_0)
- net DDR4_CH1_BG1: now also JCPU1.AY28 (DDR1_BG_1)
- net DDR4_CH1_CKE0: now also JCPU1.AY29 (DDR1_CKE_0)
- net DDR4_CH1_CKE1: now also JCPU1.AV29 (DDR1_CKE_1)
- net DDR4_CH1_CLK0+: now also JCPU1.AM20 (DDR1_CKP_0)
- net DDR4_CH1_CLK0-: now also JCPU1.AM21 (DDR1_CKN_0)
- net DDR4_CH1_CLK1+: now also JCPU1.AP22 (DDR1_CKP_1)
- net DDR4_CH1_CLK1-: now also JCPU1.AP21 (DDR1_CKN_1)
- net DDR4_CH1_CS0#: now also JCPU1.AP17 (DDR1_CS#_0)
- net DDR4_CH1_CS1#: now also JCPU1.AN15 (DDR1_CS#_1)
- net DDR4_CH1_DQ0: now also JCPU1.AD34 (DDR1_DQ_0/DDR0_DQ_16)
- net DDR4_CH1_DQ1: now also JCPU1.AD35 (DDR1_DQ_1/DDR0_DQ_17)
- net DDR4_CH1_DQ10: now also JCPU1.AK32 (DDR1_DQ_10/DDR0_DQ_26)
- net DDR4_CH1_DQ11: now also JCPU1.AL32 (DDR1_DQ_11/DDR0_DQ_27)
- net DDR4_CH1_DQ12: now also JCPU1.AK34 (DDR1_DQ_12/DDR0_DQ_28)
- net DDR4_CH1_DQ13: now also JCPU1.AL34 (DDR1_DQ_13/DDR0_DQ_29)
- net DDR4_CH1_DQ14: now also JCPU1.AK31 (DDR1_DQ_14/DDR0_DQ_30)
- net DDR4_CH1_DQ15: now also JCPU1.AL31 (DDR1_DQ_15/DDR0_DQ_31)
- net DDR4_CH1_DQ16: now also JCPU1.AP35 (DDR1_DQ_16/DDR0_DQ_48)
- net DDR4_CH1_DQ17: now also JCPU1.AN35 (DDR1_DQ_17/DDR0_DQ_49)
- net DDR4_CH1_DQ18: now also JCPU1.AN32 (DDR1_DQ_18/DDR0_DQ_50)
- net DDR4_CH1_DQ19: now also JCPU1.AP32 (DDR1_DQ_19/DDR0_DQ_51)
- net DDR4_CH1_DQ2: now also JCPU1.AG35 (DDR1_DQ_2/DDR0_DQ_18)
- net DDR4_CH1_DQ20: now also JCPU1.AN34 (DDR1_DQ_20/DDR0_DQ_52)
- net DDR4_CH1_DQ21: now also JCPU1.AP34 (DDR1_DQ_21/DDR0_DQ_53)
- net DDR4_CH1_DQ22: now also JCPU1.AN31 (DDR1_DQ_22/DDR0_DQ_54)
- net DDR4_CH1_DQ23: now also JCPU1.AP31 (DDR1_DQ_23/DDR0_DQ_55)
- net DDR4_CH1_DQ24: now also JCPU1.AL29 (DDR1_DQ_24/DDR0_DQ_56)
- net DDR4_CH1_DQ25: now also JCPU1.AM29 (DDR1_DQ_25/DDR0_DQ_57)
- net DDR4_CH1_DQ26: now also JCPU1.AP29 (DDR1_DQ_26/DDR0_DQ_58)
- net DDR4_CH1_DQ27: now also JCPU1.AR29 (DDR1_DQ_27/DDR0_DQ_59)
- net DDR4_CH1_DQ28: now also JCPU1.AM28 (DDR1_DQ_28/DDR0_DQ_60)
- net DDR4_CH1_DQ29: now also JCPU1.AL28 (DDR1_DQ_29/DDR0_DQ_61)
- net DDR4_CH1_DQ3: now also JCPU1.AH35 (DDR1_DQ_3/DDR0_DQ_19)
- net DDR4_CH1_DQ30: now also JCPU1.AR28 (DDR1_DQ_30/DDR0_DQ_62)
- net DDR4_CH1_DQ31: now also JCPU1.AP28 (DDR1_DQ_31/DDR0_DQ_63)
- net DDR4_CH1_DQ32: now also JCPU1.AR12 (DDR1_DQ_32/DDR1_DQ_16)
- net DDR4_CH1_DQ33: now also JCPU1.AP12 (DDR1_DQ_33/DDR1_DQ_17)
- net DDR4_CH1_DQ34: now also JCPU1.AM13 (DDR1_DQ_34/DDR1_DQ_18)
- net DDR4_CH1_DQ35: now also JCPU1.AL13 (DDR1_DQ_35/DDR1_DQ_19)
- net DDR4_CH1_DQ36: now also JCPU1.AR13 (DDR1_DQ_36/DDR1_DQ_20)
- net DDR4_CH1_DQ37: now also JCPU1.AP13 (DDR1_DQ_37/DDR1_DQ_21)
- net DDR4_CH1_DQ38: now also JCPU1.AM12 (DDR1_DQ_38/DDR1_DQ_22)
- net DDR4_CH1_DQ39: now also JCPU1.AL12 (DDR1_DQ_39/DDR1_DQ_23)
- net DDR4_CH1_DQ4: now also JCPU1.AE35 (DDR1_DQ_4/DDR0_DQ_20)
- net DDR4_CH1_DQ40: now also JCPU1.AP10 (DDR1_DQ_40/DDR1_DQ_24)
- net DDR4_CH1_DQ41: now also JCPU1.AR10 (DDR1_DQ_41/DDR1_DQ_25)
- net DDR4_CH1_DQ42: now also JCPU1.AR7 (DDR1_DQ_42/DDR1_DQ_26)
- net DDR4_CH1_DQ43: now also JCPU1.AP7 (DDR1_DQ_43/DDR1_DQ_27)
- net DDR4_CH1_DQ44: now also JCPU1.AR9 (DDR1_DQ_44/DDR1_DQ_28)
- net DDR4_CH1_DQ45: now also JCPU1.AP9 (DDR1_DQ_45/DDR1_DQ_29)
- net DDR4_CH1_DQ46: now also JCPU1.AR6 (DDR1_DQ_46/DDR1_DQ_30)
- net DDR4_CH1_DQ47: now also JCPU1.AP6 (DDR1_DQ_47/DDR1_DQ_31)
- net DDR4_CH1_DQ48: now also JCPU1.AM10 (DDR1_DQ_48/DDR1_DQ_48)
- net DDR4_CH1_DQ49: now also JCPU1.AL10 (DDR1_DQ_49/DDR1_DQ_49)
- net DDR4_CH1_DQ5: now also JCPU1.AE34 (DDR1_DQ_5/DDR0_DQ_21)
- net DDR4_CH1_DQ50: now also JCPU1.AM7 (DDR1_DQ_50/DDR1_DQ_50)
- net DDR4_CH1_DQ51: now also JCPU1.AL7 (DDR1_DQ_51/DDR1_DQ_51)
- net DDR4_CH1_DQ52: now also JCPU1.AM9 (DDR1_DQ_52/DDR1_DQ_52)
- net DDR4_CH1_DQ53: now also JCPU1.AL9 (DDR1_DQ_53/DDR1_DQ_53)
- net DDR4_CH1_DQ54: now also JCPU1.AM6 (DDR1_DQ_54/DDR1_DQ_54)
- net DDR4_CH1_DQ55: now also JCPU1.AL6 (DDR1_DQ_55/DDR1_DQ_55)
- net DDR4_CH1_DQ56: now also JCPU1.AJ6 (DDR1_DQ_56/DDR1_DQ_56)
- net DDR4_CH1_DQ57: now also JCPU1.AJ7 (DDR1_DQ_57/DDR1_DQ_57)
- net DDR4_CH1_DQ58: now also JCPU1.AE6 (DDR1_DQ_58/DDR1_DQ_58)
- net DDR4_CH1_DQ59: now also JCPU1.AF7 (DDR1_DQ_59/DDR1_DQ_59)
- net DDR4_CH1_DQ6: now also JCPU1.AG34 (DDR1_DQ_6/DDR0_DQ_22)
- net DDR4_CH1_DQ60: now also JCPU1.AH7 (DDR1_DQ_60/DDR1_DQ_60)
- net DDR4_CH1_DQ61: now also JCPU1.AH6 (DDR1_DQ_61/DDR1_DQ_61)
- net DDR4_CH1_DQ62: now also JCPU1.AE7 (DDR1_DQ_62/DDR1_DQ_62)
- net DDR4_CH1_DQ63: now also JCPU1.AF6 (DDR1_DQ_63/DDR1_DQ_63)
- net DDR4_CH1_DQ7: now also JCPU1.AH34 (DDR1_DQ_7/DDR0_DQ_23)
- net DDR4_CH1_DQ8: now also JCPU1.AK35 (DDR1_DQ_8/DDR0_DQ_24)
- net DDR4_CH1_DQ9: now also JCPU1.AL35 (DDR1_DQ_9/DDR0_DQ_25)
- net DDR4_CH1_DQS0+: now also JCPU1.AF35 (DDR1_DQSP_0/DDR0_DQSP_2)
- net DDR4_CH1_DQS0-: now also JCPU1.AF34 (DDR1_DQSN_0/DDR0_DQSN_2)
- net DDR4_CH1_DQS1+: now also JCPU1.AL33 (DDR1_DQSP_1/DDR0_DQSP_3)
- net DDR4_CH1_DQS1-: now also JCPU1.AK33 (DDR1_DQSN_1/DDR0_DQSN_3)
- net DDR4_CH1_DQS2+: now also JCPU1.AP33 (DDR1_DQSP_2/DDR0_DQSP_6)
- net DDR4_CH1_DQS2-: now also JCPU1.AN33 (DDR1_DQSN_2/DDR0_DQSN_6)
- net DDR4_CH1_DQS3+: now also JCPU1.AN28 (DDR1_DQSP_3/DDR0_DQSP_7)
- net DDR4_CH1_DQS3-: now also JCPU1.AN29 (DDR1_DQSN_3/DDR0_DQSN_7)
- net DDR4_CH1_DQS4+: now also JCPU1.AN12 (DDR1_DQSP_4/DDR1_DQSP_2)
- net DDR4_CH1_DQS4-: now also JCPU1.AN13 (DDR1_DQSN_4/DDR1_DQSN_2)
- net DDR4_CH1_DQS5+: now also JCPU1.AP8 (DDR1_DQSP_5/DDR1_DQSP_3)
- net DDR4_CH1_DQS5-: now also JCPU1.AR8 (DDR1_DQSN_5/DDR1_DQSN_3)
- net DDR4_CH1_DQS6+: now also JCPU1.AL8 (DDR1_DQSP_6/DDR1_DQSP_6)
- net DDR4_CH1_DQS6-: now also JCPU1.AM8 (DDR1_DQSN_6/DDR1_DQSN_6)
- net DDR4_CH1_DQS7+: now also JCPU1.AG7 (DDR1_DQSP_7/DDR1_DQSP_7)
- net DDR4_CH1_DQS7-: now also JCPU1.AG6 (DDR1_DQSN_7/DDR1_DQSN_7)
- net DDR4_CH1_DQS8+: now also JCPU1.AN25 (DDR1_DQSP_8/DDR1_DQSP_8)
- net DDR4_CH1_DQS8-: now also JCPU1.AN26 (DDR1_DQSN_8/DDR1_DQSN_8)
- net DDR4_CH1_ECC0: now also JCPU1.AR25 (DDR1_ECC_0)
- net DDR4_CH1_ECC1: now also JCPU1.AR26 (DDR1_ECC_1)
- net DDR4_CH1_ECC2: now also JCPU1.AM26 (DDR1_ECC_2)
- net DDR4_CH1_ECC3: now also JCPU1.AM25 (DDR1_ECC_3)
- net DDR4_CH1_ECC4: now also JCPU1.AP26 (DDR1_ECC_4)
- net DDR4_CH1_ECC5: now also JCPU1.AP25 (DDR1_ECC_5)
- net DDR4_CH1_ECC6: now also JCPU1.AL25 (DDR1_ECC_6)
- net DDR4_CH1_ECC7: now also JCPU1.AL26 (DDR1_ECC_7)
- net DDR4_CH1_ODT0: now also JCPU1.AM16 (DDR1_ODT_0)
- net DDR4_CH1_ODT1: now also JCPU1.AL16 (DDR1_ODT_1)
- net DDR4_CH1_Parity: now also JCPU1.AL20 (DDR1_PAR)
